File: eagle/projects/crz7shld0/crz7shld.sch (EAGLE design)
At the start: 52 parts, among them IC1 IS62WV51216BLL-55T, J1 HDR-2X6, J2 HDR-2X6, J3 HDR-2X8, J4 HDR-2X3, J5 HDR-2X8, J6 HDR-2X6, J7 HDR-2X6, Q2 BSS138, Q3 BSS138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

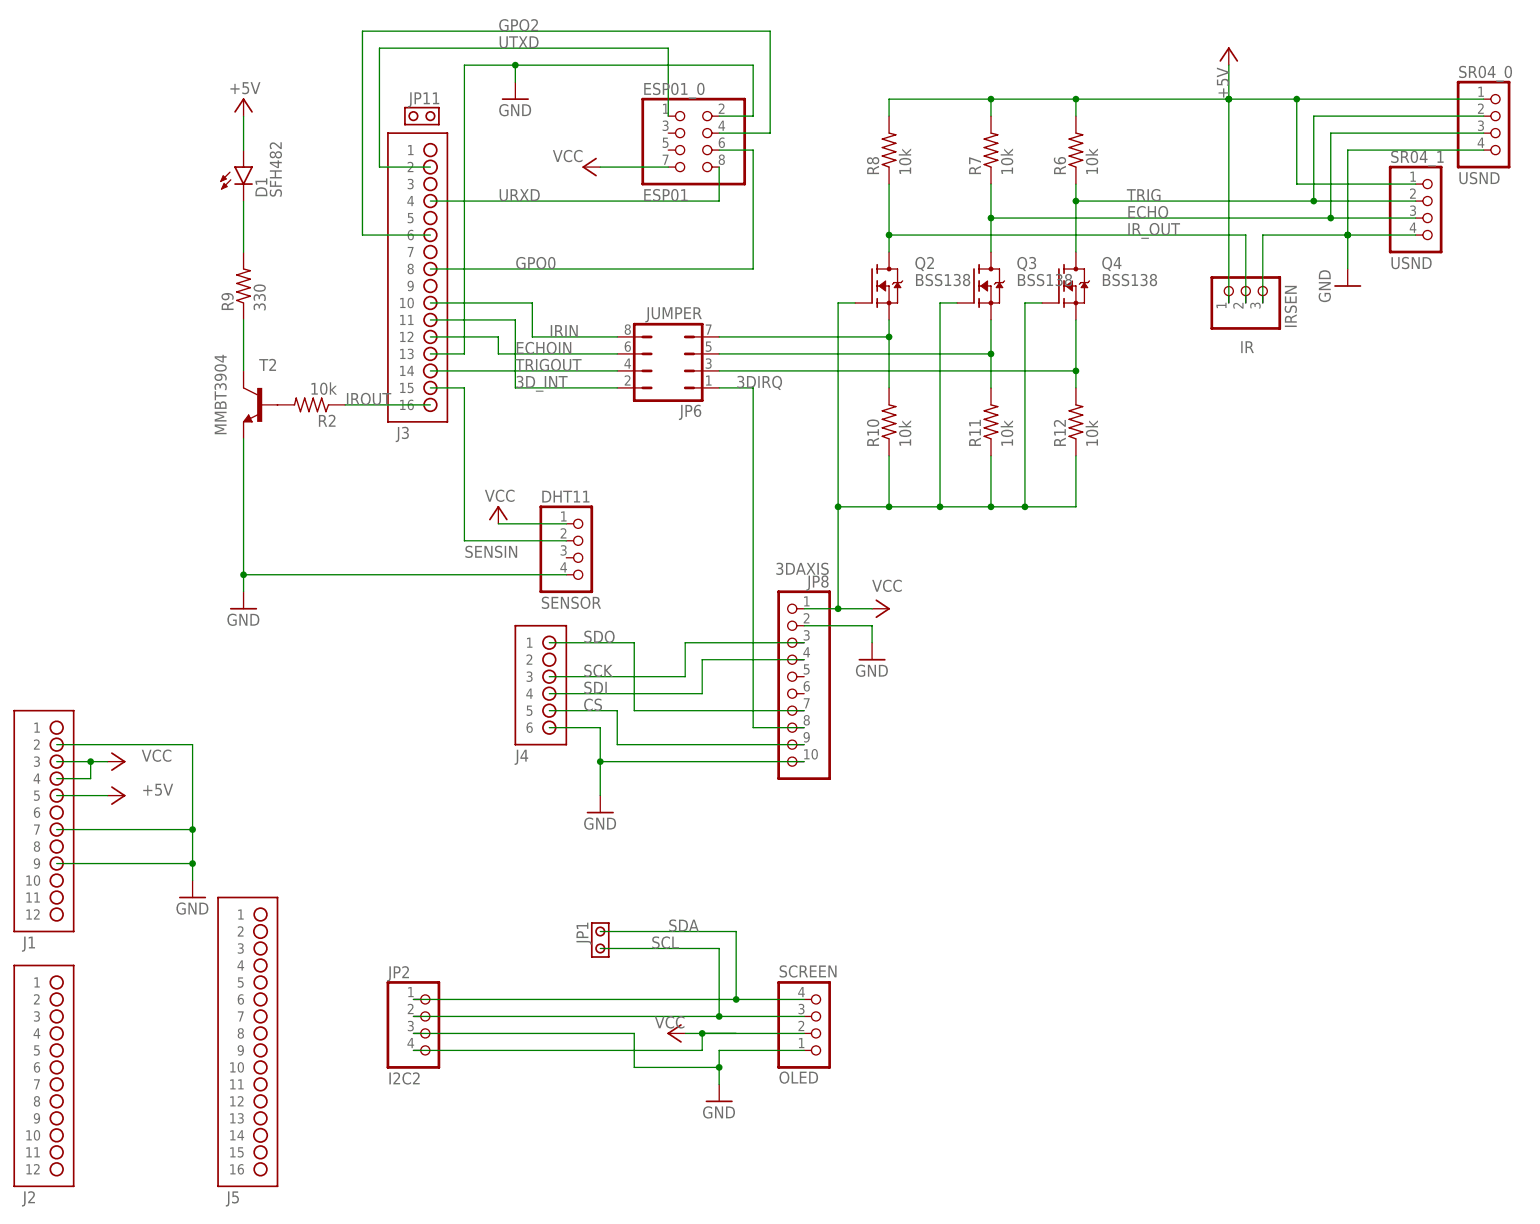
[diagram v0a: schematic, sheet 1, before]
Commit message: order JLCPCB crz7shld1
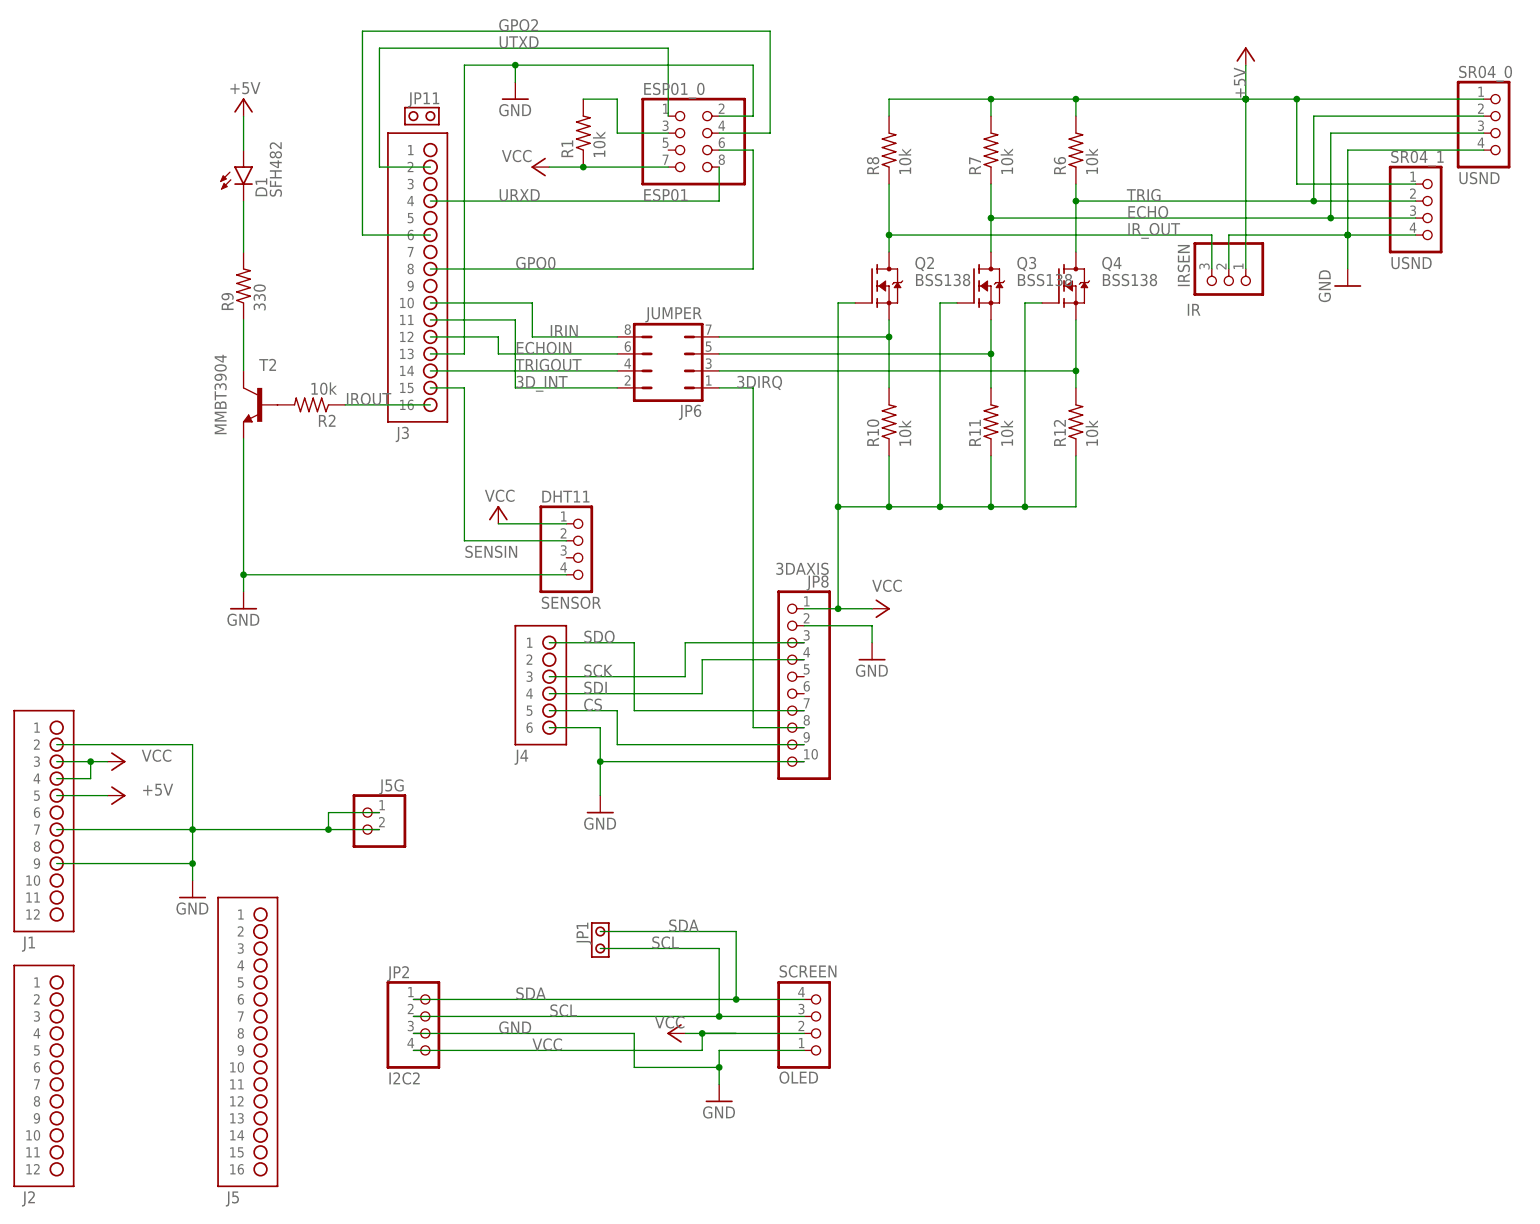
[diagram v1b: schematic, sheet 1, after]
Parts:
- added J5G: (no value), pinhead2:PINHD-1X2
- added R1, R13, R15, R16: 10k, rcl:R-US_R0402
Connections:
- new net N$10: ESP01_3.3, R16.1
- new net N$6: ESP01_0.3, R1.2
- new net N$8: ESP01_2.3, R13.1
- new net N$9: ESP01_1.3, R15.2
- net GND: now also IR.2, J5G.1, J5G.2; no longer IR.3
- net IR_OUT: now also IR.3; no longer IR.2
- net VCC: now also R1.1
- net VCC2ND: now also R15.1
- net VCC3RD: now also R16.2
- net VCCLAT: now also R13.2
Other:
- moved on the sheet: IR
